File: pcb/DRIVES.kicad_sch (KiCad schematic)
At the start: 0 parts

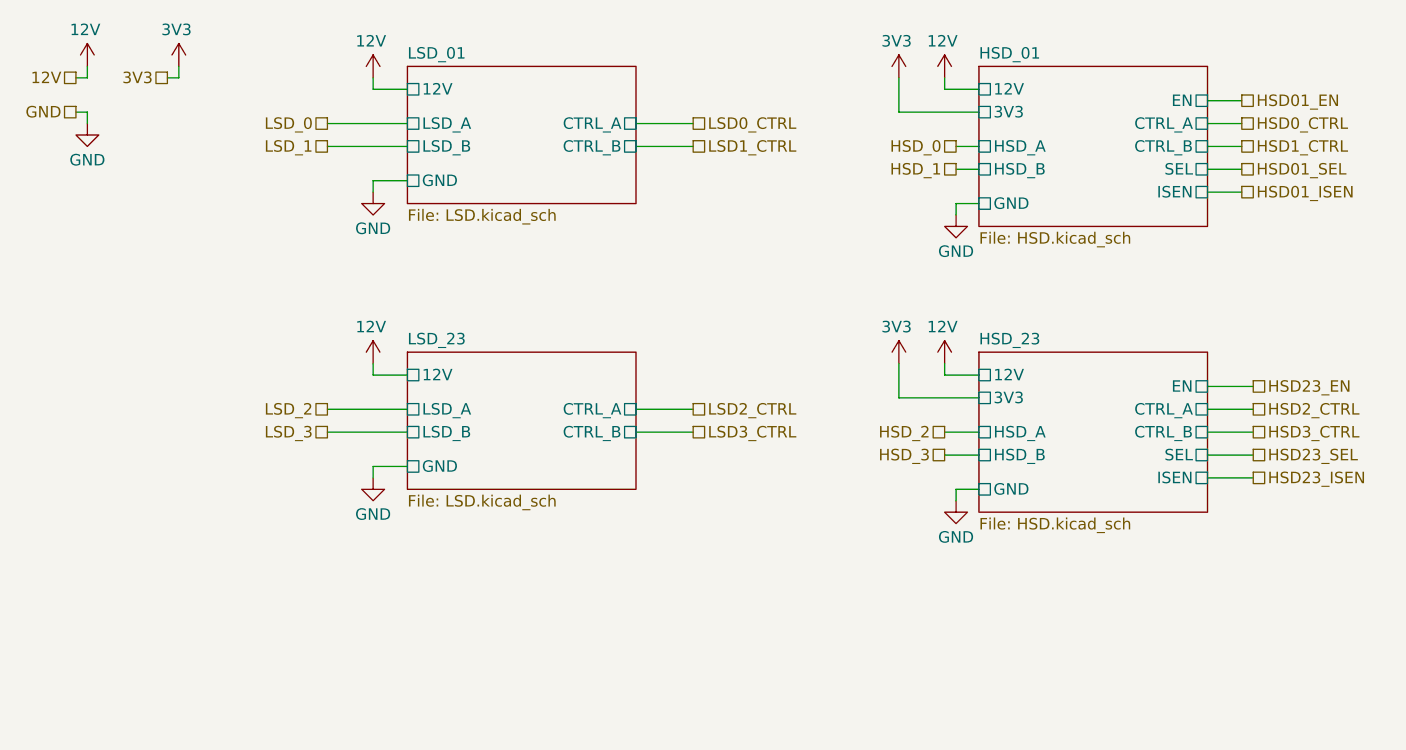
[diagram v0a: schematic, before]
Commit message: added better lsds
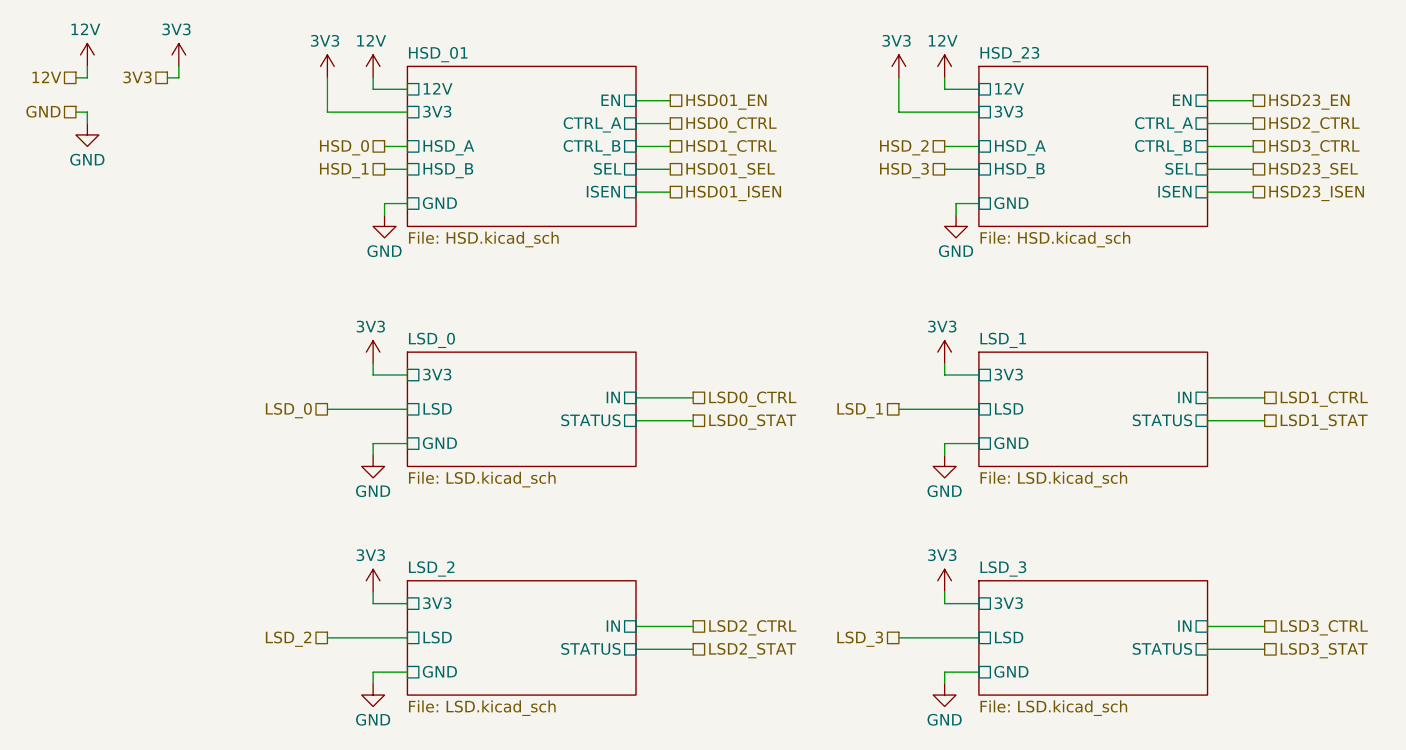
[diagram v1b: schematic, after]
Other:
- sheet LSD_01 renamed LSD_0
- removed sheet LSD_23
- added sheet LSD_1 (LSD.kicad_sch)
- added sheet LSD_2 (LSD.kicad_sch)
- added sheet LSD_3 (LSD.kicad_sch)
- sheet LSD_0 ports: added 3V3, IN, LSD, STATUS; removed 12V, CTRL_A, CTRL_B, LSD_A, LSD_B
